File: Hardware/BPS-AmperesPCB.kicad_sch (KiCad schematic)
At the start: 54 parts, among them IC1 INA241A5IDR, IC5 AMC1350DWVR, J1 Discharge V_In, J2 PeripheralCAN, J3 Charge V_In, J4 PeripheralCAN, J5 Shunt Conn, U1 INA145UA/2K5, U2 AMC1300BDWV, U6 TLV6001DCK, U7 TLV6001DCK

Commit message: is this how you TVS
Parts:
- removed C27, C28: 1uF, symbol Device:C_Small
- removed C3: 2.2uF, Capacitor_SMD:C_0805_2012Metric, symbol Device:C_Small
- removed R4, R6: 2.4k, Resistor_SMD:R_0805_2012Metric, symbol Device:R_Small_US
- removed TP13: OUT+, symbol Connector:TestPoint
- removed TP14: OUT-, symbol Connector:TestPoint
- removed U2: AMC1300BDWV, Package_SO:SOIC-8_7.5x5.85mm_P1.27mm, symbol Amplifier_Difference:AMC1300BDWV
- added D10: VCU TVS, Diode_SMD:D_SOD-123F, symbol Device:D_Zener
- added D5, D6: TVS, symbol Device:D_Zener
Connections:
- net +3.3V: now also D5.1 (K)
- net GND: now also D6.2 (A)
- net I_OUT: now also D5.2 (A), D6.1 (K)
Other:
- note added: "Fixed Gain: 0.4 V/V Target Input Voltage Range: 0.1 - 3.2 V Target Output Voltage Range: 0.04 - 1.28 V"
- note added: "Gain: 100 V/V Target Input Voltage: Reference voltage (bias for discharge): 1.3 V - (70A * 250 uOhm * 100)V + Vref = 3.05 V - (-32 * 250 uOhm * 100)V + Vref = 0.5 V Maximum current range: -44 to +80A (0.1V to 3.2V)"
- note added: "Gain: 2.5 V/V (may change) Vout = 2.5(VoutP - VoutN) Target Output voltage range: 0.1 - 3.2 V Cutoff freq: TBD"
- note added: "TODO: - use full 5V input for AMC1350: output is 0 to 2V or - just amplify after isolation? <---- maybe this one"
- note added: "TODO: spec TVS diode TVS from VCU for reference (use this?)"
- note removed: "Difference amp Vout = (R2/R1) * (Vp - Vn)"
- note removed: "Gain: 0.4 V/V Target Input Voltage Range: 0.1 - 3.2 V Target Output Voltage Range: 0.04 - 1.28 V"
- note removed: "Gain: 2.5 V/V (??) Vout = 2.5(VoutP - VoutN) Cutoff freq: TBD Target Output voltage range: 0.1 - 3.2 V"
- note removed: "Gain: TBD Max input voltage: -5 to 110V Max current:"
- note removed: "Input Voltage Range: +- 0.25 V"
- note removed: "Output Voltage Range: Fixed gain: 8.2"
- note removed: "Reference voltage (bias for discharge): 1.3 V - (70A * 250 uOhm * 100)V + Vref = 3.05 V - (-32 * 250 uOhm * 100)V + Vref = 0.5 V - Maximum range: -44 to +80A (0.1V to 3.2V)"
- note removed: "TODO: - use full 5V input for AMC1350: output is 0 to 2V or - just amplify after isolation?"
- moved on the sheet: C1, C2, C4, D1, D2, R3, R5, R7, R8, R9, U1, VOut1

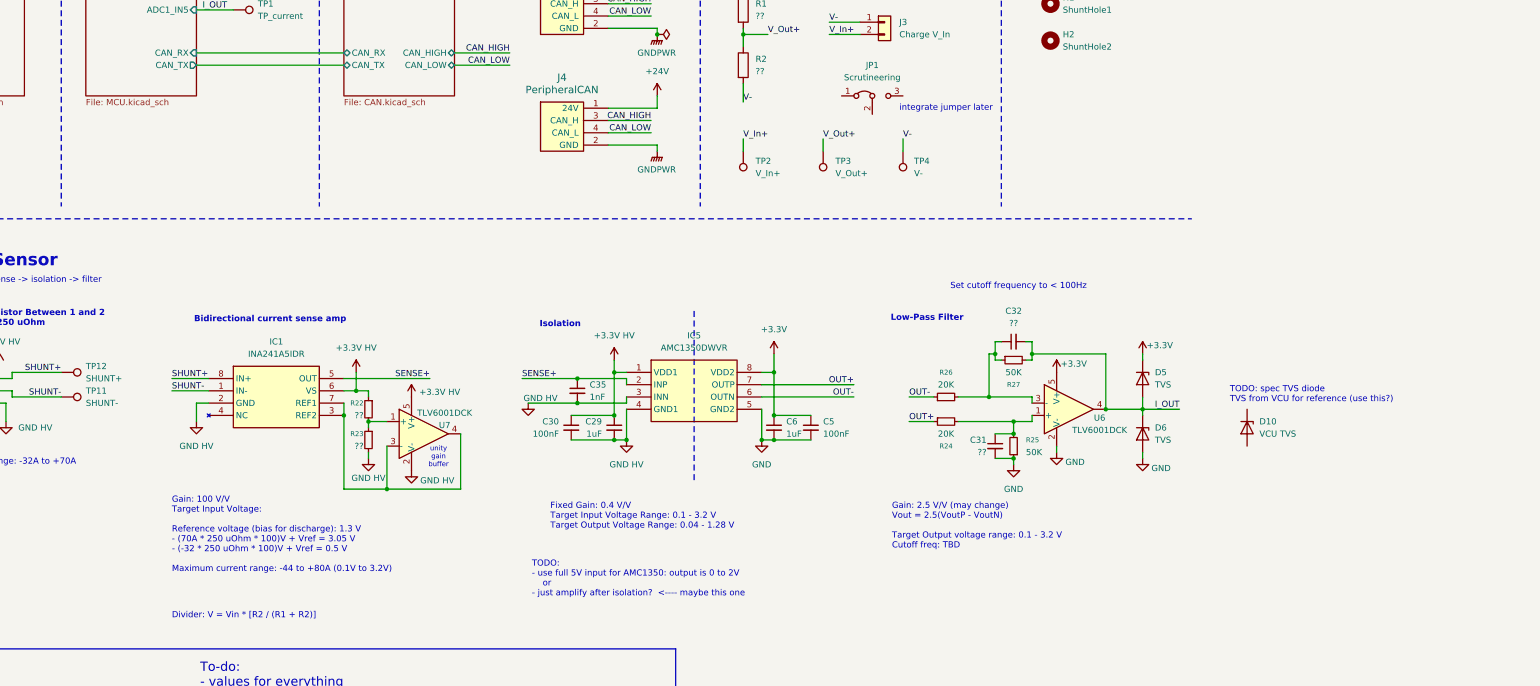
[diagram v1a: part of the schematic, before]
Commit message: changed to TI generated filter
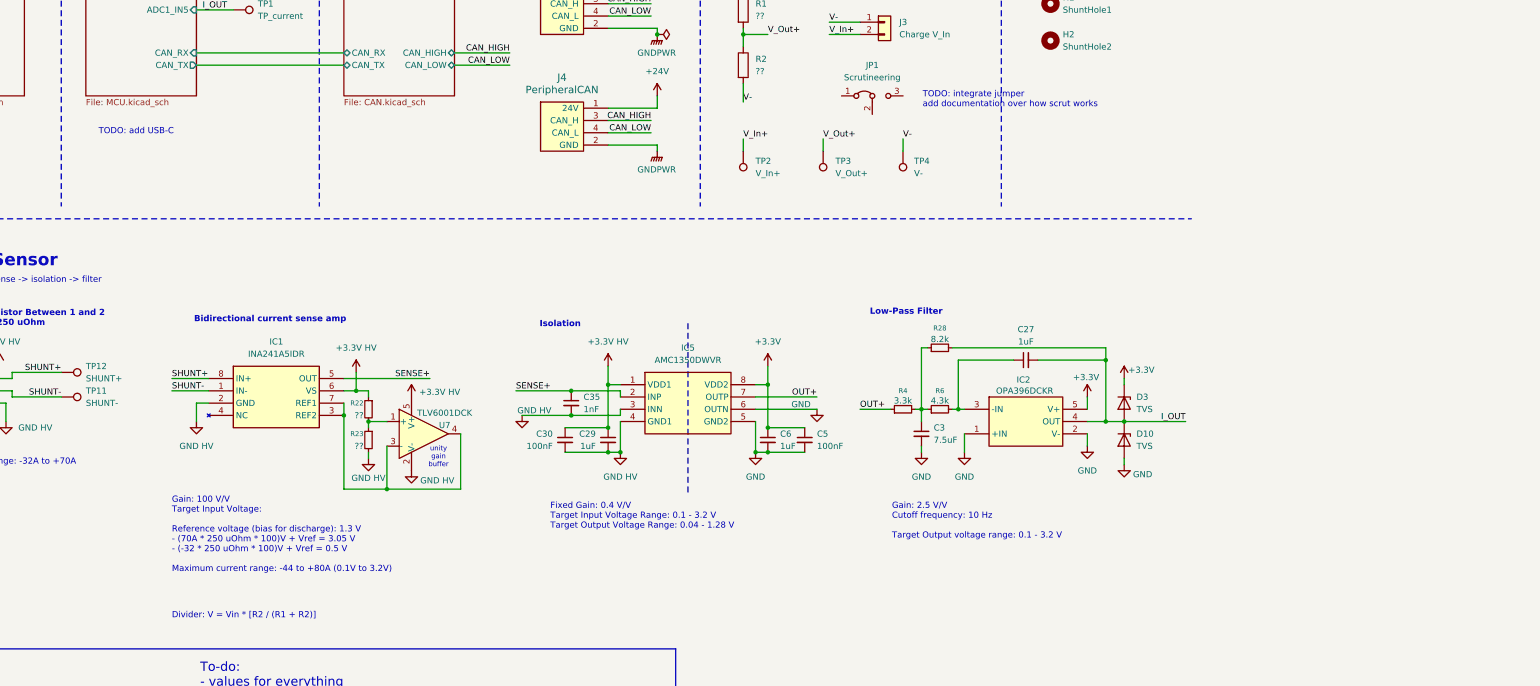
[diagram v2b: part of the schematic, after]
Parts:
- removed C31, C32: ??, symbol Device:C_Small
- removed D5, D6: TVS, symbol Device:D_Zener
- removed R24, R26: 20K, symbol Device:R_Small
- removed R25, R27: 50K, symbol Device:R_Small
- removed U6: TLV6001DCK, Package_TO_SOT_SMD:SOT-353_SC-70-5, symbol Amplifier_Operational:TLV6001DCK
- added C27: 1uF, symbol Device:C_Small
- added C3: 7.5uF, symbol Device:C_Small
- added D3: TVS, Diode_SMD:D_SOD-123F, symbol Device:D_Zener
- added IC2: OPA396DCKR, SOT65P210X110-5N, symbol OPA396DCKR:OPA396DCKR
- added R28: 8.2k, symbol Device:R_Small
- added R4: 3.3k, symbol Device:R_Small
- added R6: 4.3k, symbol Device:R_Small
- D10: value VCU TVS -> TVS
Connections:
- net OUT- is gone; now on net GND: IC5.6 (OUTN)
- net +3.3V: now also D3.1 (K), IC2.5 (V+)
- net GND: now also D10.2 (A), C3.2, IC2.1 (+IN), IC2.2 (V-)
- net I_OUT: now also D10.1 (K), C27.2, D3.2 (A), IC2.4 (OUT), R28.2
- net OUT+: now also R4.1
- new net: C3.1, R28.1, R4.2, R6.1
- new net: C27.1, IC2.3 (-IN), R6.2
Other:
- note added: "Gain: 2.5 V/V Cutoff frequency: 10 Hz Target Output voltage range: 0.1 - 3.2 V"
- note added: "TODO: add USB-C"
- note added: "TODO: integrate jumper add documentation over how scrut works"
- note removed: "Gain: 2.5 V/V (may change) Vout = 2.5(VoutP - VoutN) Target Output voltage range: 0.1 - 3.2 V Cutoff freq: TBD"
- note removed: "TODO: - use full 5V input for AMC1350: output is 0 to 2V or - just amplify after isolation? <---- maybe this one"
- note removed: "TODO: spec TVS diode TVS from VCU for reference (use this?)"
- note removed: "integrate jumper later"
- moved on the sheet: C29, C30, C35, C5, C6, D10, IC5

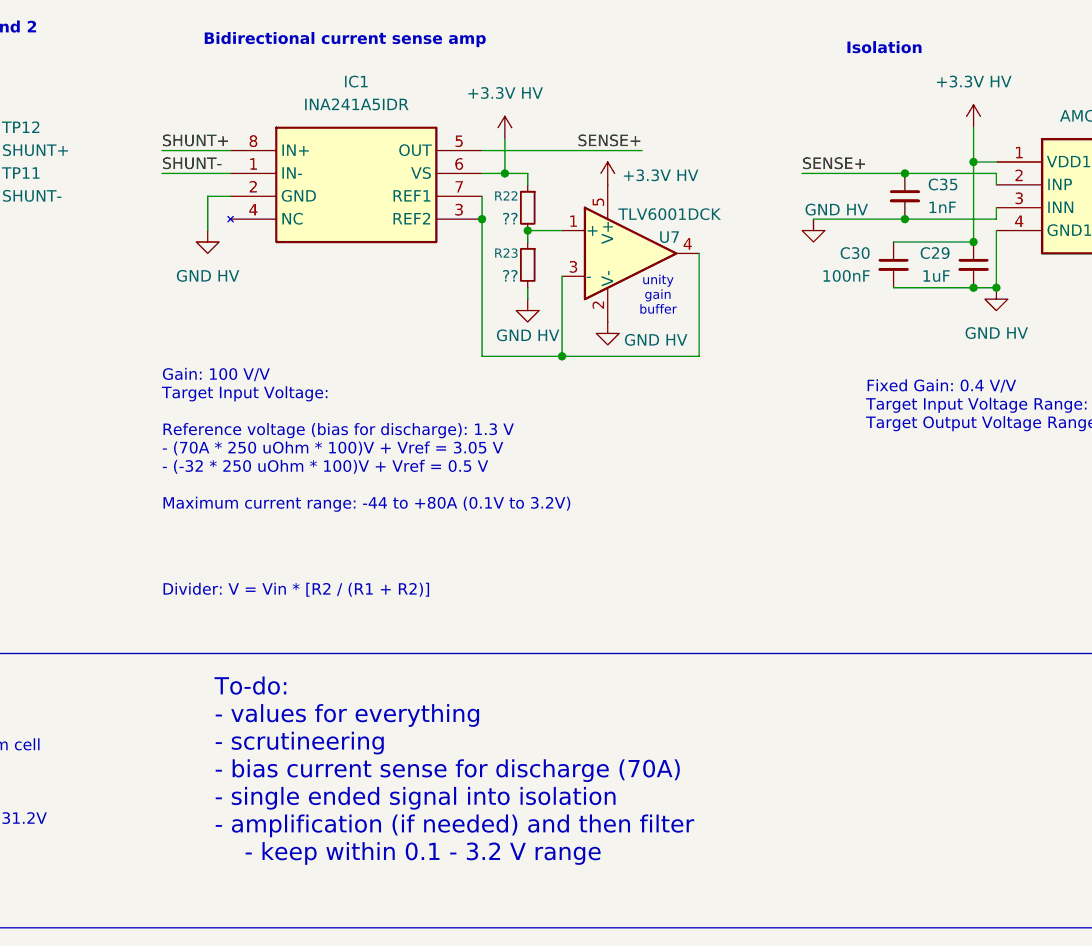
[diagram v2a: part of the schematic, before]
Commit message: set reference voltage for current sense
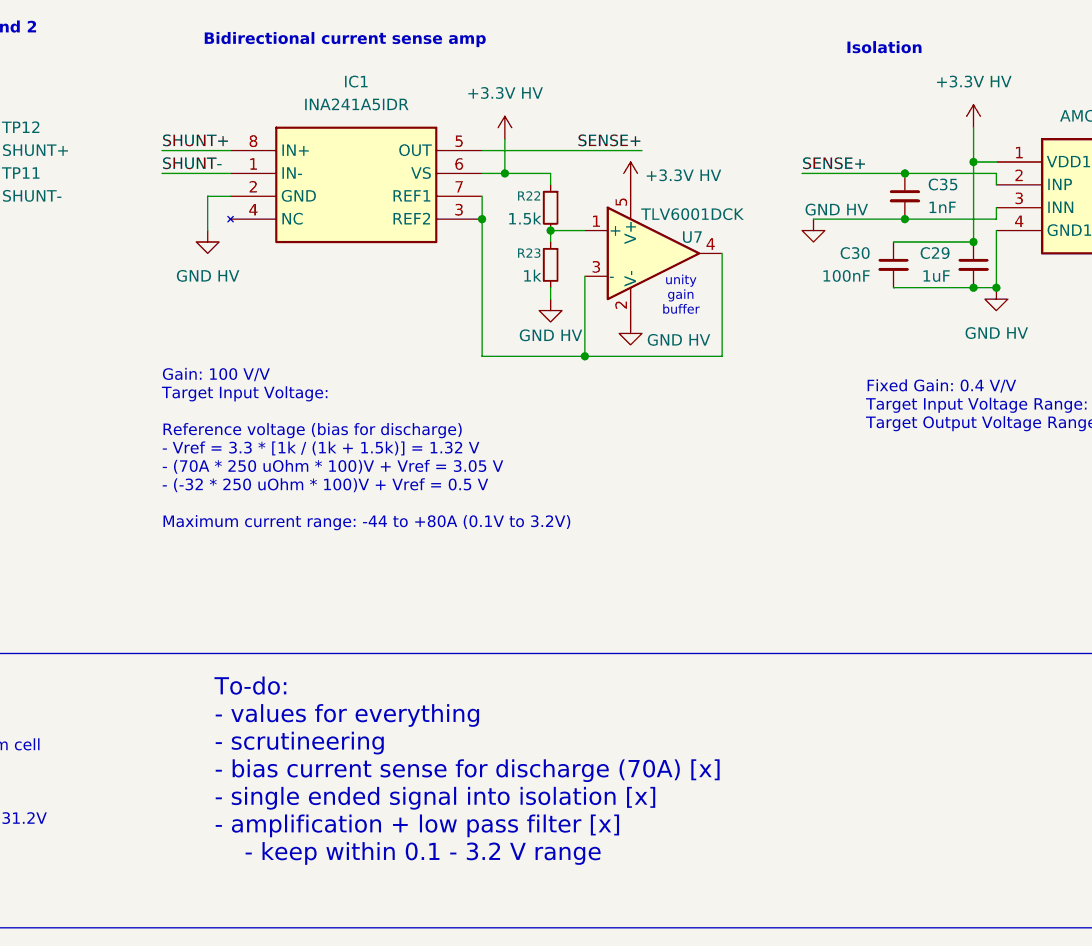
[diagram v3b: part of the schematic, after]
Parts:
- R22: value ?? -> 1.5k
- R23: value ?? -> 1k
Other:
- note added: "Gain: 100 V/V Target Input Voltage: Reference voltage (bias for discharge) - Vref = 3.3 * [1k / (1k + 1.5k)] = 1.32 V - (70A * 250 uOhm * 100)V + Vref = 3.05 V - (-32 * 250 uOhm * 100)V + Vref = 0.5 V Maximum current range: -44 to +80A (0.1V to 3.2V)"
- note added: "To-do: - values for everything - scrutineering - bias current sense for discharge (70A) [x] - single ended signal into isolation [x] - amplification + low pass filter [x] - keep within 0.1 - 3.2 V range"
- note removed: "Divider: V = Vin * [R2 / (R1 + R2)]"
- note removed: "Gain: 100 V/V Target Input Voltage: Reference voltage (bias for discharge): 1.3 V - (70A * 250 uOhm * 100)V + Vref = 3.05 V - (-32 * 250 uOhm * 100)V + Vref = 0.5 V Maximum current range: -44 to +80A (0.1V to 3.2V)"
- note removed: "To-do: - values for everything - scrutineering - bias current sense for discharge (70A) - single ended signal into isolation - amplification (if needed) and then filter - keep within 0.1 - 3.2 V range"
- moved on the sheet: R22, R23, U7
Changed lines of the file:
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@@
 	(text "unity\ngain\nbuffer"
 		(exclude_from_sim no)
-		(at 126.238 125.476 0)
+		(at 128.778 125.476 0)
 		(effects
 			(font
@@
 		)
 	)
-	(text "Gain: 100 V/V\nTarget Input Voltage: \n\nReference voltage (bias for discharge): 1.3 V\n- (70A * 250 uOhm * 100)V + Vref = 3.05 V\n- (-32 * 250 uOhm * 100)V + Vref = 0.5 V\n\nMaximum current range: -44 to +80A (0.1V to 3.2V)"
+	(text "Gain: 100 V/V\nTarget Input Voltage: \n\nReference voltage (bias for discharge)\n- Vref = 3.3 * [1k / (1k + 1.5k)] = 1.32 V\n- (70A * 250 uOhm * 100)V + Vref = 3.05 V\n- (-32 * 250 uOhm * 100)V + Vref = 0.5 V\n\nMaximum current range: -44 to +80A (0.1V to 3.2V)"
 		(exclude_from_sim no)
 		(at 71.12 133.604 0)
@@
 		)
 	)
-	(text "Divider: V = Vin * [R2 / (R1 + R2)]"
-		(exclude_from_sim no)
-		(at 71.12 157.48 0)
-		(effects
-			(font
-				(size 1.27 1.27)
-			)
-			(justify left top)
-		)
-	)
 	(text "Current Range:\nCharge (-): 32A thru Elcon; max 54A from cell\nDischarge (+): 70A\n\nVoltage Range:\n32 cells, 2.6 - 4.1 V range => 83.2V to 131.2V"
 		(exclude_from_sim no)
@@
 		)
 	)
-	(text "To-do:\n- values for everything\n- scrutineering\n- bias current sense for discharge (70A)\n- single ended signal into isolation\n- amplification (if needed) and then filter\n	- keep within 0.1 - 3.2 V range"
+	(text "To-do:\n- values for everything\n- scrutineering\n- bias current sense for discharge (70A) [x]\n- single ended signal into isolation [x]\n- amplification + low pass filter [x]\n	- keep within 0.1 - 3.2 V range"
 		(exclude_from_sim no)
 		(at 76.962 167.894 0)
@@
 	)
 	(junction
-		(at 115.57 132.08)
+		(at 118.11 132.08)
 		(diameter 0)
 		(color 0 0 0 0)
@@
 	)
 	(junction
-		(at 111.76 118.11)
+		(at 114.3 118.11)
 		(diameter 0)
 		(color 0 0 0 0)
@@
 	(wire
 		(pts
-			(xy 111.76 118.11) (xy 115.57 118.11)
+			(xy 114.3 118.11) (xy 118.11 118.11)
 		)
 		(stroke
@@
 	(wire
 		(pts
-			(xy 106.68 132.08) (xy 115.57 132.08)
+			(xy 106.68 132.08) (xy 118.11 132.08)
 		)
 		(stroke
@@
 	(wire
 		(pts
-			(xy 106.68 116.84) (xy 106.68 132.08)
-		)
-		(stroke
-			(width 0)
-			(type default)
-		)
-	)
-	(wire
-		(pts
 			(xy 161.29 60.96) (xy 171.45 60.96)
 		)
@@
 	(wire
 		(pts
-			(xy 111.76 125.73) (xy 111.76 124.46)
+			(xy 114.3 125.73) (xy 114.3 124.46)
 		)
 		(stroke
@@
 		)
 	)
+	(wire
+		(pts
+			(xy 106.68 116.84) (xy 106.68 132.08)
+		)
+		(stroke
+			(width 0)
+			(type default)
+		)
+	)
 	(polyline
 		(pts
@@
 	(wire
 		(pts
-			(xy 111.76 118.11) (xy 111.76 119.38)
+			(xy 114.3 118.11) (xy 114.3 119.38)
 		)
 		(stroke
@@
 	(wire
 		(pts
-			(xy 130.81 120.65) (xy 130.81 132.08)
+			(xy 133.35 120.65) (xy 133.35 132.08)
 		)
 		(stroke
@@
 	(wire
 		(pts
-			(xy 115.57 123.19) (xy 115.57 132.08)
+			(xy 118.11 123.19) (xy 118.11 132.08)
 		)
 		(stroke
@@
 	(wire
 		(pts
-			(xy 109.22 111.76) (xy 111.76 111.76)
+			(xy 109.22 111.76) (xy 114.3 111.76)
 		)
 		(stroke
@@
 	(wire
 		(pts
-			(xy 111.76 113.03) (xy 111.76 111.76)
+			(xy 114.3 113.03) (xy 114.3 111.76)
 		)
 		(stroke
@@
 	(wire
 		(pts
-			(xy 115.57 132.08) (xy 130.81 132.08)
+			(xy 118.11 132.08) (xy 133.35 132.08)
 		)
 		(stroke
@@
 	(symbol
 		(lib_id "power:GND")
-		(at 120.65 128.27 0)
+		(at 123.19 128.27 0)
 		(unit 1)
 		(exclude_from_sim no)
@@
 		(dnp no)
 		(property "Reference" "#PWR086"
-			(at 120.65 134.62 0)
+			(at 123.19 134.62 0)
 			(effects
 				(font
@@
 		)
 		(property "Value" "GND HV"
-			(at 125.984 130.302 0)
+			(at 128.524 130.302 0)
 			(effects
 				(font
@@
 		)
 		(property "Footprint" ""
-			(at 120.65 128.27 0)
+			(at 123.19 128.27 0)
 			(effects
 				(font
@@
 		)
 		(property "Datasheet" ""
-			(at 120.65 128.27 0)
+			(at 123.19 128.27 0)
 			(effects
 				(font
@@
 		)
 		(property "Description" "Power symbol creates a global label with name \"GND\" , ground"
-			(at 120.65 128.27 0)
+			(at 123.19 128.27 0)
 			(effects
 				(font
@@
 	(symbol
 		(lib_id "Device:R_Small")
-		(at 111.76 121.92 0)
+		(at 114.3 121.92 0)
 		(mirror y)
 		(unit 1)
@@
 		(dnp no)
 		(property "Reference" "R23"
-			(at 110.744 120.65 0)
+			(at 113.284 120.65 0)
 			(effects
 				(font
@@
 			)
 		)
-		(property "Value" "??"
-			(at 110.744 123.19 0)
+		(property "Value" "1k"
+			(at 113.284 123.19 0)
 			(effects
 				(font
@@
 		)
 		(property "Footprint" ""
-			(at 111.76 121.92 0)
+			(at 114.3 121.92 0)
 			(effects
 				(font
@@
 		)
 		(property "Datasheet" "~"
-			(at 111.76 121.92 0)
+			(at 114.3 121.92 0)
 			(effects
 				(font
@@
 		)
 		(property "Description" "Resistor, small symbol"
-			(at 111.76 121.92 0)
+			(at 114.3 121.92 0)
 			(effects
 				(font
@@
 	(symbol
 		(lib_id "Device:R_Small")
-		(at 111.76 115.57 0)
+		(at 114.3 115.57 0)
 		(mirror y)
 		(unit 1)
@@
 		(dnp no)
 		(property "Reference" "R22"
-			(at 110.744 114.3 0)
+			(at 113.284 114.3 0)
 			(effects
 				(font
@@
 			)
 		)
-		(property "Value" "??"
-			(at 110.744 116.84 0)
+		(property "Value" "1.5k"
+			(at 113.284 116.84 0)
 			(effects
 				(font
@@
 		)
 		(property "Footprint" ""
-			(at 111.76 115.57 0)
+			(at 114.3 115.57 0)
 			(effects
 				(font
@@
 		)
 		(property "Datasheet" "~"
-			(at 111.76 115.57 0)
+			(at 114.3 115.57 0)
 			(effects
 				(font
@@
 		)
 		(property "Description" "Resistor, small symbol"
-			(at 111.76 115.57 0)
+			(at 114.3 115.57 0)
 			(effects
 				(font
@@
 	(symbol
 		(lib_id "power:+3.3V")
-		(at 120.65 113.03 0)
+		(at 123.19 113.03 0)
 		(unit 1)
 		(exclude_from_sim no)
@@
 		(dnp no)
 		(property "Reference" "#PWR079"
-			(at 120.65 116.84 0)
+			(at 123.19 116.84 0)
 			(effects
 				(font
@@
 		)
 		(property "Value" "+3.3V HV"
-			(at 126.492 112.014 0)
+			(at 129.032 112.014 0)
 			(effects
 				(font
@@
 		)
 		(property "Footprint" ""
-			(at 120.65 113.03 0)
+			(at 123.19 113.03 0)
 			(effects
 				(font
@@
 		)
 		(property "Datasheet" ""
-			(at 120.65 113.03 0)
+			(at 123.19 113.03 0)
 			(effects
 				(font
@@
 		)
 		(property "Description" "Power symbol creates a global label with name \"+3.3V\""
-			(at 120.65 113.03 0)
+			(at 123.19 113.03 0)
 			(effects
 				(font
@@
 		(lib_name "TLV6001DCK_1")
 		(lib_id "Amplifier_Operational:TLV6001DCK")
-		(at 120.65 120.65 0)
+		(at 123.19 120.65 0)
 		(unit 1)
 		(exclude_from_sim no)
@@
 		(dnp no)
 		(property "Reference" "U7"
-			(at 127.508 118.872 0)
+			(at 130.048 118.872 0)
 			(effects
 				(font
@@
 		)
 		(property "Value" "TLV6001DCK"
-			(at 127.508 116.332 0)
+			(at 130.048 116.332 0)
 			(effects
 				(font
@@
 		)
 		(property "Footprint" "Package_TO_SOT_SMD:SOT-353_SC-70-5"
-			(at 125.73 120.65 0)
+			(at 128.27 120.65 0)
 			(effects
 				(font
@@
 		)
 		(property "Datasheet" "http://www.ti.com/lit/ds/symlink/tlv6001.pdf"
-			(at 120.65 120.65 0)
+			(at 123.19 120.65 0)
 			(effects
 				(font
@@
 		)
 		(property "Description" "Low-power, Rail-to-rail, 1MHz Operational Amplifier, SOT-353"
-			(at 120.65 120.65 0)
+			(at 123.19 120.65 0)
 			(effects
 				(font
@@
 	(symbol
 		(lib_id "power:GND")
-		(at 111.76 125.73 0)
+		(at 114.3 125.73 0)
 		(unit 1)
 		(exclude_from_sim no)
@@
 		(dnp no)
 		(property "Reference" "#PWR072"
-			(at 111.76 132.08 0)
+			(at 114.3 132.08 0)
 			(effects
 				(font
@@
 		)
 		(property "Value" "GND HV"
-			(at 111.76 129.794 0)
+			(at 114.3 129.794 0)
 			(effects
 				(font
@@
 		)
 		(property "Footprint" ""
-			(at 111.76 125.73 0)
+			(at 114.3 125.73 0)
 			(effects
 				(font
@@
 		)
 		(property "Datasheet" ""
-			(at 111.76 125.73 0)
+			(at 114.3 125.73 0)
 			(effects
 				(font
@@
 		)
 		(property "Description" "Power symbol creates a global label with name \"GND\" , ground"
-			(at 111.76 125.73 0)
+			(at 114.3 125.73 0)
 			(effects
 				(font
